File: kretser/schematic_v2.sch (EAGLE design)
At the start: 17 parts, among them IC1 ATMEGA168-20PU, U2 LM2940CT-5.0/NOPB

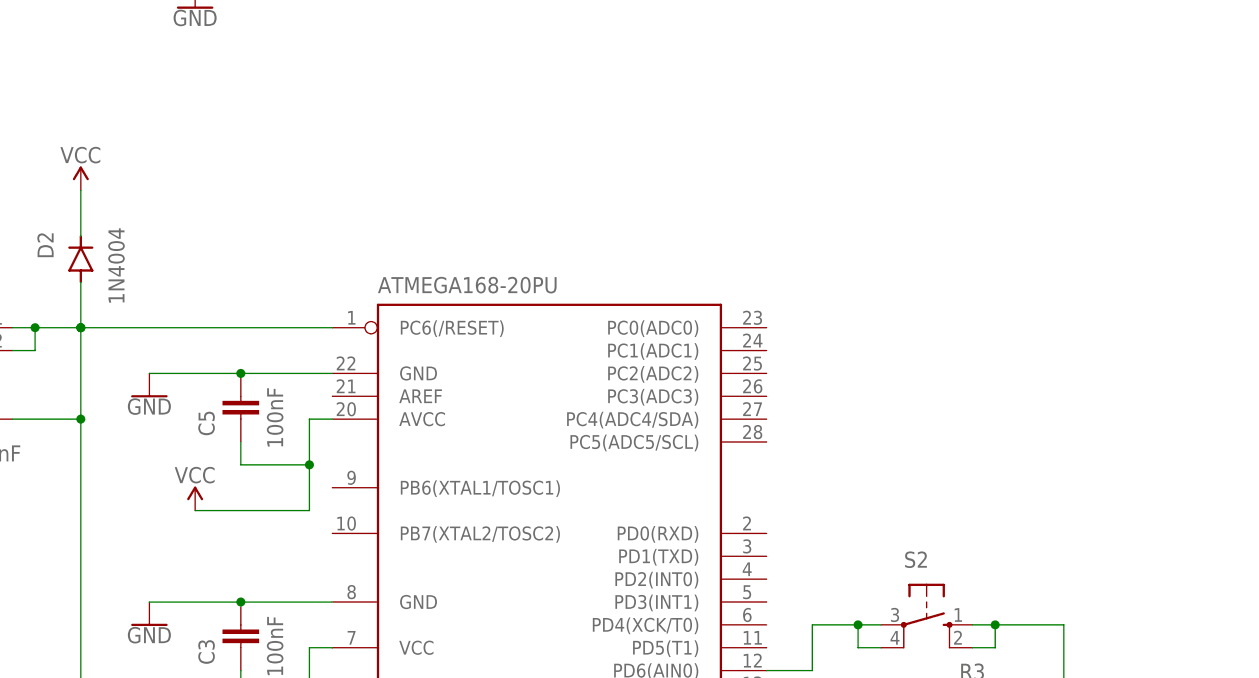
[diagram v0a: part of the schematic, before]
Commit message: added ADC to krets
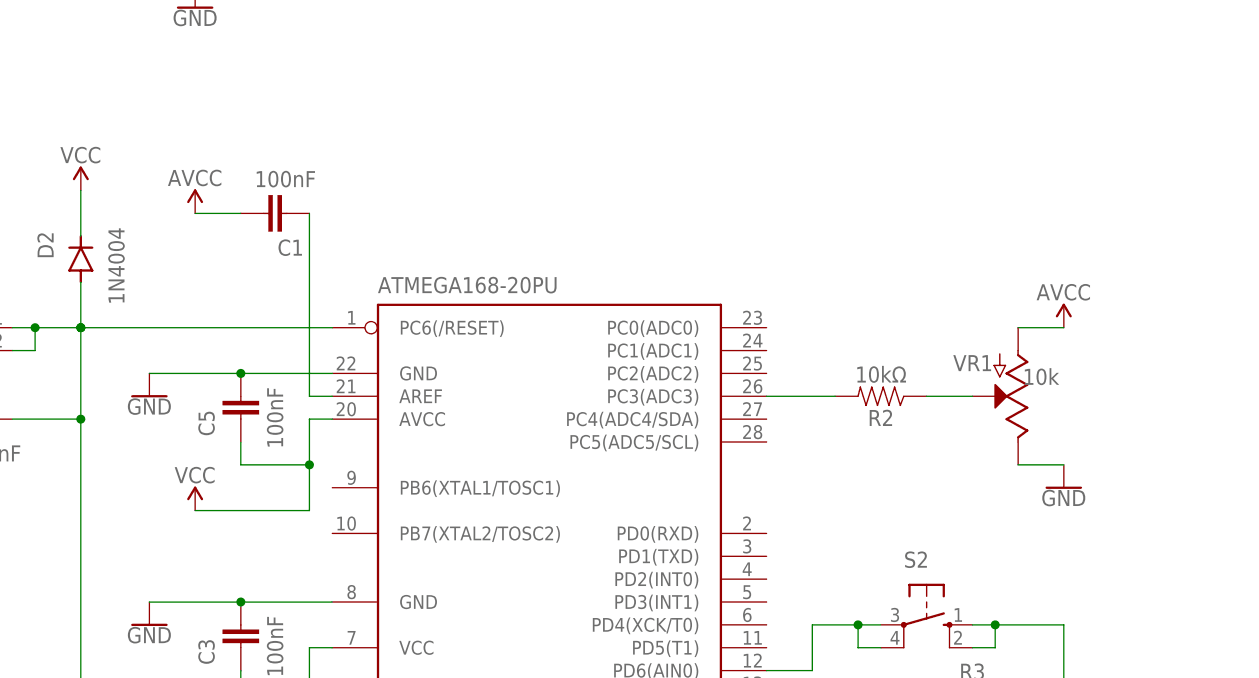
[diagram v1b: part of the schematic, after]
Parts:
- added C1: 100nF, SparkFun-Capacitors:470PF-0603-50V-5%
- added R2: 10kΩ, SparkFun-Resistors:10OHM-HORIZ-1/4W-1%
- added VR1: 10k, SparkFun-Resistors:POTENTIOMETER-PTH-9MM-1/20W-20%-KIT
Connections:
- new net N$10: C1.1, IC1.AREF
- new net N$5: IC1.PC3(ADC3), R2.2
- new net N$9: R2.1, VR1.S
- net GND: now also VR1.E
- net VCC: now also C1.2, VR1.A
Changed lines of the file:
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@@
 <part name="R1" library="SparkFun-Resistors" library_urn="urn:adsk.eagle:library:532" deviceset="10OHM" device="-HORIZ-1/4W-1%" package3d_urn="urn:adsk.eagle:package:39658/2" value="330Ω"/>
 <part name="SUPPLY2" library="SparkFun-PowerSymbols" library_urn="urn:adsk.eagle:library:530" deviceset="VCC" device="" value="VCC"/>
+<part name="VR1" library="SparkFun-Resistors" library_urn="urn:adsk.eagle:library:532" deviceset="POTENTIOMETER" device="-PTH-9MM-1/20W-20%-KIT" package3d_urn="urn:adsk.eagle:package:39674/2" value="10k"/>
+<part name="R2" library="SparkFun-Resistors" library_urn="urn:adsk.eagle:library:532" deviceset="10OHM" device="-HORIZ-1/4W-1%" package3d_urn="urn:adsk.eagle:package:39658/2" value="10kΩ"/>
+<part name="GND9" library="SparkFun-PowerSymbols" library_urn="urn:adsk.eagle:library:530" deviceset="GND" device=""/>
+<part name="SUPPLY7" library="SparkFun-PowerSymbols" library_urn="urn:adsk.eagle:library:530" deviceset="VCC" device="" value="AVCC"/>
+<part name="SUPPLY8" library="SparkFun-PowerSymbols" library_urn="urn:adsk.eagle:library:530" deviceset="VCC" device="" value="AVCC"/>
+<part name="C1" library="SparkFun-Capacitors" library_urn="urn:adsk.eagle:library:510" deviceset="470PF" device="-0603-50V-5%" package3d_urn="urn:adsk.eagle:package:41385090/1" value="100nF"/>
 </parts>
 <sheets>
@@
 <attribute name="VALUE" x="81.28" y="98.806" size="1.778" layer="96" font="vector" rot="R180" align="bottom-center"/>
 </instance>
+<instance part="VR1" gate="G$1" x="172.72" y="106.68" smashed="yes" rot="R180">
+<attribute name="NAME" x="169.926" y="111.252" size="1.778" layer="95" font="vector" rot="R180"/>
+<attribute name="VALUE" x="175.26" y="107.95" size="1.778" layer="95" font="vector" align="bottom-center"/>
+</instance>
+<instance part="R2" gate="G$1" x="157.48" y="106.68" smashed="yes" rot="R180">
+<attribute name="NAME" x="157.48" y="105.156" size="1.778" layer="95" font="vector" rot="R180" align="bottom-center"/>
+<attribute name="VALUE" x="157.48" y="108.204" size="1.778" layer="96" font="vector" rot="R180" align="top-center"/>
+</instance>
+<instance part="GND9" gate="1" x="177.8" y="96.52" smashed="yes">
+<attribute name="VALUE" x="177.8" y="96.266" size="1.778" layer="96" font="vector" align="top-center"/>
+</instance>
+<instance part="SUPPLY7" gate="G$1" x="177.8" y="114.3" smashed="yes">
+<attribute name="VALUE" x="177.8" y="119.126" size="1.778" layer="96" font="vector" rot="R180" align="bottom-center"/>
+</instance>
+<instance part="SUPPLY8" gate="G$1" x="81.28" y="127" smashed="yes">
+<attribute name="VALUE" x="81.28" y="131.826" size="1.778" layer="96" font="vector" rot="R180" align="bottom-center"/>
+</instance>
+<instance part="C1" gate="G$1" x="88.9" y="127" smashed="yes" rot="R270">
+<attribute name="NAME" x="90.424" y="122.301" size="1.778" layer="95" font="vector"/>
+<attribute name="VALUE" x="87.884" y="129.921" size="1.778" layer="96" font="vector"/>
+</instance>
 </instances>
 <busses>
@@
 <wire x1="86.36" y1="83.82" x2="76.2" y2="83.82" width="0.1524" layer="91"/>
 <junction x="86.36" y="83.82"/>
+</segment>
+<segment>
+<pinref part="GND9" gate="1" pin="GND"/>
+<pinref part="VR1" gate="G$1" pin="E"/>
+<wire x1="177.8" y1="99.06" x2="172.72" y2="99.06" width="0.1524" layer="91"/>
 </segment>
 </net>
@@
 <junction x="93.98" y="99.06"/>
 </segment>
+<segment>
+<pinref part="SUPPLY7" gate="G$1" pin="VCC"/>
+<pinref part="VR1" gate="G$1" pin="A"/>
+<wire x1="177.8" y1="114.3" x2="172.72" y2="114.3" width="0.1524" layer="91"/>
+</segment>
+<segment>
+<pinref part="SUPPLY8" gate="G$1" pin="VCC"/>
+<pinref part="C1" gate="G$1" pin="2"/>
+<wire x1="81.28" y1="127" x2="86.36" y2="127" width="0.1524" layer="91"/>
+</segment>
 </net>
 <net name="V_IN1" class="0">
@@
 </segment>
 </net>
+<net name="N$5" class="0">
+<segment>
+<pinref part="IC1" gate="G$1" pin="PC3(ADC3)"/>
+<wire x1="144.78" y1="106.68" x2="152.4" y2="106.68" width="0.1524" layer="91"/>
+<pinref part="R2" gate="G$1" pin="2"/>
+</segment>
+</net>
+<net name="N$9" class="0">
+<segment>
+<pinref part="VR1" gate="G$1" pin="S"/>
+<pinref part="R2" gate="G$1" pin="1"/>
+<wire x1="167.64" y1="106.68" x2="162.56" y2="106.68" width="0.1524" layer="91"/>
+</segment>
+</net>
+<net name="N$10" class="0">
+<segment>
+<pinref part="IC1" gate="G$1" pin="AREF"/>
+<wire x1="96.52" y1="106.68" x2="93.98" y2="106.68" width="0.1524" layer="91"/>
+<wire x1="93.98" y1="106.68" x2="93.98" y2="127" width="0.1524" layer="91"/>
+<pinref part="C1" gate="G$1" pin="1"/>
+</segment>
+</net>

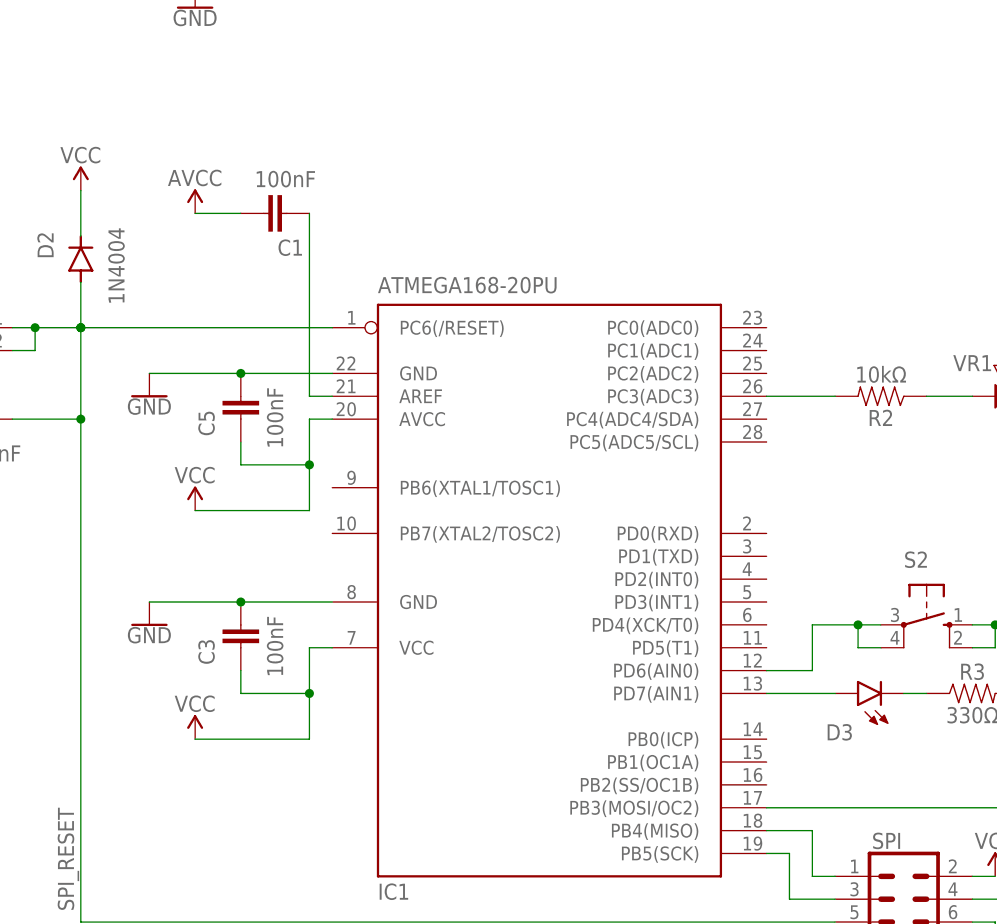
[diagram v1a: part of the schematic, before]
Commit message: finished ADC code and updated krets for LED and Aref capacitator
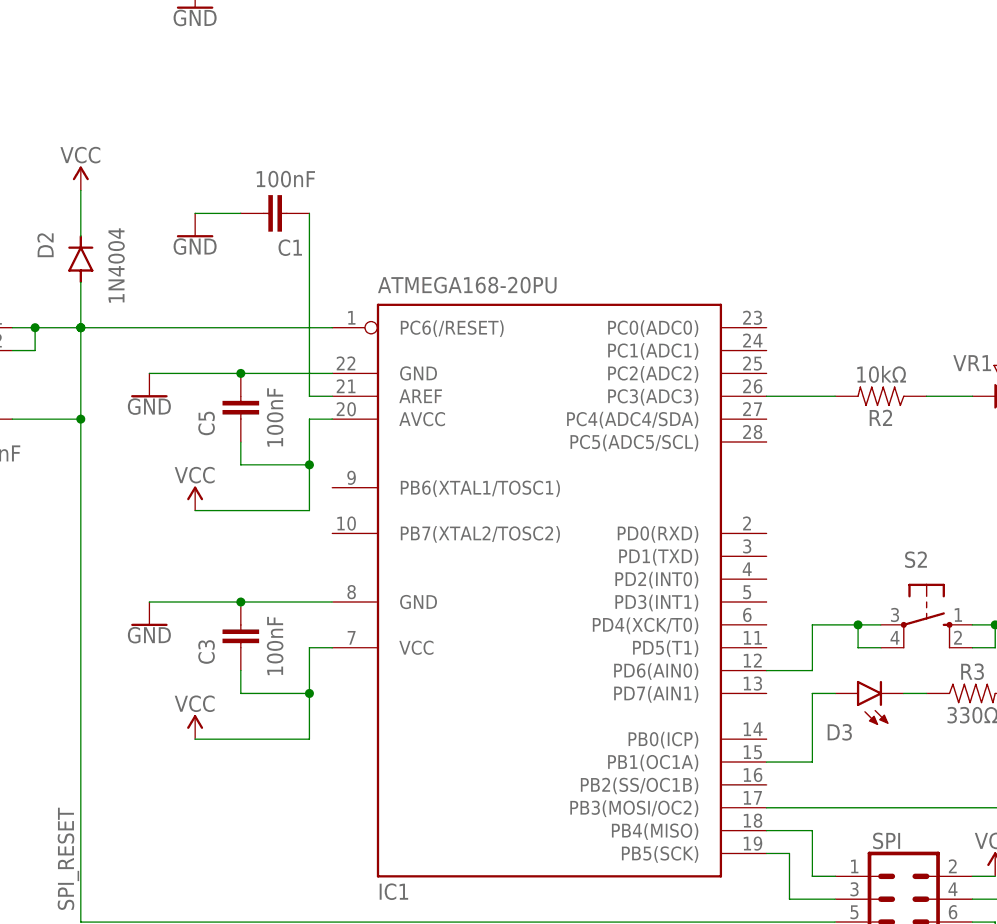
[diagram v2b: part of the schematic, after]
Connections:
- net GND: now also C1.2
- net N$4: now also IC1.PB1(OC1A); no longer IC1.PD7(AIN1)
- net VCC: no longer C1.2
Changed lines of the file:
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@@
 <part name="GND9" library="SparkFun-PowerSymbols" library_urn="urn:adsk.eagle:library:530" deviceset="GND" device=""/>
 <part name="SUPPLY7" library="SparkFun-PowerSymbols" library_urn="urn:adsk.eagle:library:530" deviceset="VCC" device="" value="AVCC"/>
-<part name="SUPPLY8" library="SparkFun-PowerSymbols" library_urn="urn:adsk.eagle:library:530" deviceset="VCC" device="" value="AVCC"/>
 <part name="C1" library="SparkFun-Capacitors" library_urn="urn:adsk.eagle:library:510" deviceset="470PF" device="-0603-50V-5%" package3d_urn="urn:adsk.eagle:package:41385090/1" value="100nF"/>
+<part name="GND10" library="SparkFun-PowerSymbols" library_urn="urn:adsk.eagle:library:530" deviceset="GND" device=""/>
 </parts>
 <sheets>
@@
 <attribute name="VALUE" x="177.8" y="119.126" size="1.778" layer="96" font="vector" rot="R180" align="bottom-center"/>
 </instance>
-<instance part="SUPPLY8" gate="G$1" x="81.28" y="127" smashed="yes">
-<attribute name="VALUE" x="81.28" y="131.826" size="1.778" layer="96" font="vector" rot="R180" align="bottom-center"/>
-</instance>
 <instance part="C1" gate="G$1" x="88.9" y="127" smashed="yes" rot="R270">
 <attribute name="NAME" x="90.424" y="122.301" size="1.778" layer="95" font="vector"/>
 <attribute name="VALUE" x="87.884" y="129.921" size="1.778" layer="96" font="vector"/>
+</instance>
+<instance part="GND10" gate="1" x="81.28" y="124.46" smashed="yes">
+<attribute name="VALUE" x="81.28" y="124.206" size="1.778" layer="96" font="vector" align="top-center"/>
 </instance>
 </instances>
@@
 <pinref part="VR1" gate="G$1" pin="E"/>
 <wire x1="177.8" y1="99.06" x2="172.72" y2="99.06" width="0.1524" layer="91"/>
+</segment>
+<segment>
+<pinref part="C1" gate="G$1" pin="2"/>
+<wire x1="81.28" y1="127" x2="86.36" y2="127" width="0.1524" layer="91"/>
+<pinref part="GND10" gate="1" pin="GND"/>
 </segment>
 </net>
@@
 </segment>
 </net>
-<net name="N$4" class="0">
-<segment>
-<pinref part="IC1" gate="G$1" pin="PD7(AIN1)"/>
-<pinref part="D3" gate="D1" pin="A"/>
-<wire x1="144.78" y1="73.66" x2="152.4" y2="73.66" width="0.1524" layer="91"/>
-</segment>
-</net>
 <net name="N$1" class="0">
 <segment>
@@
 <wire x1="177.8" y1="114.3" x2="172.72" y2="114.3" width="0.1524" layer="91"/>
 </segment>
-<segment>
-<pinref part="SUPPLY8" gate="G$1" pin="VCC"/>
-<pinref part="C1" gate="G$1" pin="2"/>
-<wire x1="81.28" y1="127" x2="86.36" y2="127" width="0.1524" layer="91"/>
-</segment>
 </net>
 <net name="V_IN1" class="0">
@@
 </segment>
 </net>
+<net name="N$4" class="0">
+<segment>
+<pinref part="D3" gate="D1" pin="A"/>
+<wire x1="152.4" y1="73.66" x2="149.86" y2="73.66" width="0.1524" layer="91"/>
+<wire x1="149.86" y1="73.66" x2="149.86" y2="66.04" width="0.1524" layer="91"/>
+<pinref part="IC1" gate="G$1" pin="PB1(OC1A)"/>
+<wire x1="149.86" y1="66.04" x2="144.78" y2="66.04" width="0.1524" layer="91"/>
+</segment>
+</net>
